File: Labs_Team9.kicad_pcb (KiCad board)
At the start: 2 copper layers, 101.7 x 39.2 mm, 51 parts, among them J1 Conn_02x04_Counter_Clockwise, J2 Conn_01x03_Pin, J3 Conn_01x04_Pin, J4 Conn_01x04_Pin, J5 USB_C_Receptacle_PowerOnly_6P, SW1 SW_Push, SW2 SW_Push, SW3 SW_Push, SW4 SW_Push, SW5 SW_Push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

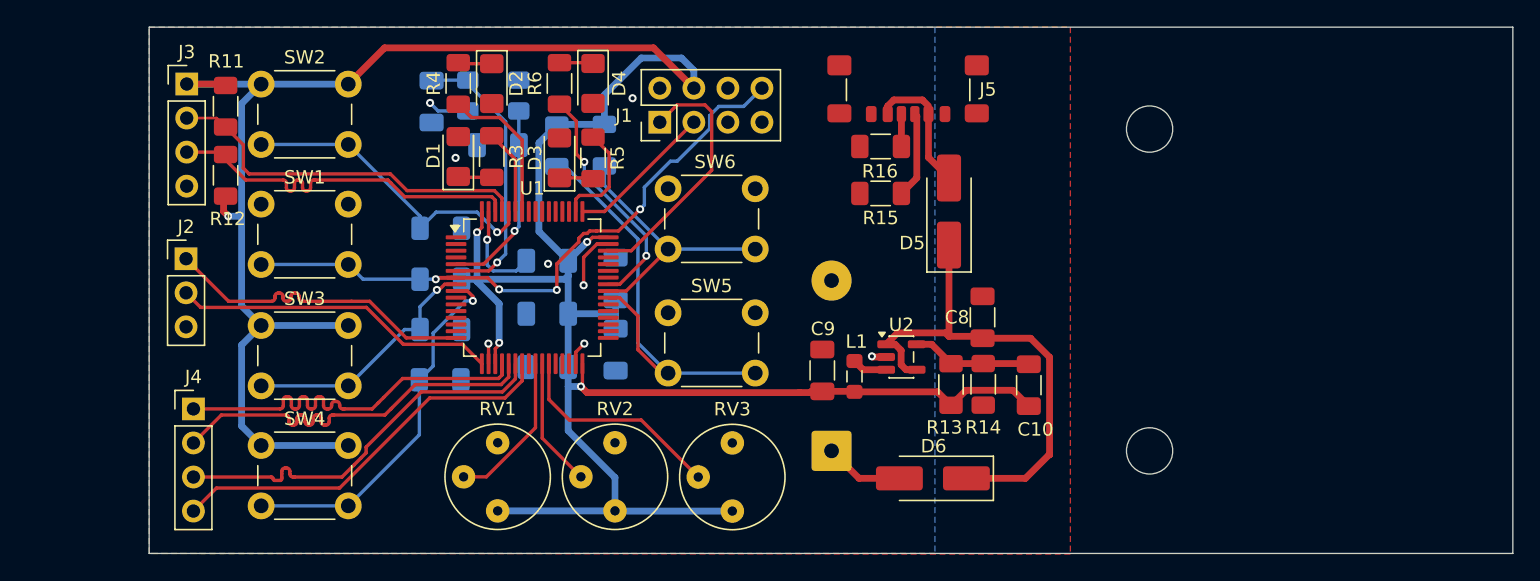
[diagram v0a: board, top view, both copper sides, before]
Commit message: lab5: add full tracing
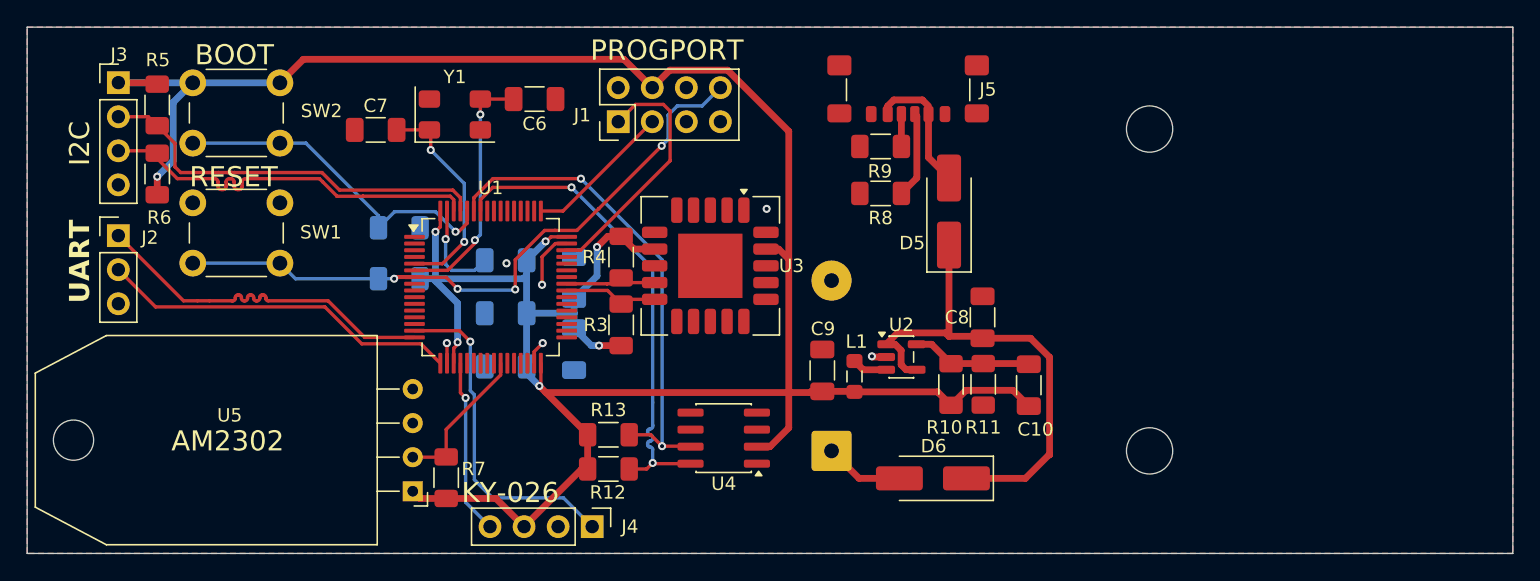
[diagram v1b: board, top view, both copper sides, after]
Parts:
- removed D1, D2, D3, D4: LED, LED_SMD:LED_1206_3216Metric_Pad1.42x1.75mm_HandSolder
- removed the R10 at (159.0, 90.2)
- removed the R5 at (158.2, 91.2)
- removed the R6 at (155.7, 85.7)
- removed the R8 at (146.8, 107.8)
- removed the R9 at (155.4, 90.3)
- removed RV1, RV2, RV3: R_Potentiometer, Potentiometer_THT:Potentiometer_Bourns_3339P_Vertical_HandSoldering
- removed SW3, SW4, SW5, SW6: SW_Push, Buttons_Switches_THT:SW_PUSH_6mm
- added R12: 2.2 kOhm, Resistor_SMD:R_1206_3216Metric_Pad1.30x1.75mm_HandSolder, F.Cu at (159.3, 114.4)
- added R13: 2.2 kOhm, Resistor_SMD:R_1206_3216Metric_Pad1.30x1.75mm_HandSolder, F.Cu at (159.3, 111.8)
- added U3: SCD40-D-R2, Sensor:Sensirion_SCD4x-1EP_10.1x10.1mm_P1.25mm_EP4.8x4.8mm, F.Cu at (166.9, 99.2)
- added U4: DS3231MZ, Package_SO:SOIC-8_3.9x4.9mm_P1.27mm, F.Cu at (167.9, 112.1)
- added U5: AM2302, Sensor:ASAIR_AM2302_P2.54mm_Lead2.75mm_TabDown, F.Cu at (144.7, 116.1)
- C6, C7, Y1: moved to F.Cu
- R3: value 510 Ohm -> 10 kOhm
- R4: value 680 Ohm -> 10 kOhm
- R7: value 10 kOhm -> 5.1 kOhm; moved to F.Cu
- moved J4 31.0 mm to (158.1, 118.7), turned to -90 degrees
- moved R4 17.8 mm to (160.2, 98.6), turned to -90 degrees
- moved R3 15.8 mm to (160.2, 103.7), turned to 90 degrees
- moved R7 11.1 mm to (147.2, 115.0), turned to 90 degrees
- moved C7 9.19 mm to (141.9, 89.1)
- moved C6 7.68 mm to (153.8, 86.8), turned to 180 degrees
- moved J2 5.34 mm to (122.8, 97.0)
- moved J3 5.10 mm to (122.8, 85.6)
- moved R5 5.10 mm to (125.7, 87.2)
- moved R6 5.10 mm to (125.7, 92.4)
- moved SW1 5.10 mm to (128.3, 94.5)
- moved SW2 5.10 mm to (134.8, 90.1)
- moved Y1 3.19 mm to (147.8, 88.0), turned to 0 degrees
- moved C2 3.10 mm to (151.6, 102.8)
- moved R2 3.10 mm to (143.7, 96.4)
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- renumbered R13 to R10, R14 to R11, R11 to R5, R12 to R6, R15 to R8, R16 to R9
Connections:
- J4 pad 1: SPI_NSS -> FLAME_ADC
- J4 pad 2: SPI_SCK -> GND
- J4 pad 3: SPI_MISO -> +3.3V
- J4 pad 4: SPI_MOSI -> FLAME_DATA
- R3 pad 1: Led_Green -> +3.3V
- R3 pad 2: Net-(D1-K) -> I2C2_SDA
- R4 pad 1: Led_Orange -> +3.3V
- R4 pad 2: Net-(D2-K) -> I2C2_SCL
- R7 pad 1: USERB1 -> +3.3V
- R7 pad 2: GND -> DATA_AM2302
- U1 pad 15: unconnected-(U1-PA1-Pad15) -> FLAME_ADC
- U1 pad 20: SPI_NSS -> FLAME_DATA
- U1 pad 21: SPI_SCK -> unconnected-(U1-PA5-Pad21)
- U1 pad 22: SPI_MISO -> unconnected-(U1-PA6-Pad22)
- U1 pad 23: SPI_MOSI -> unconnected-(U1-PA7-Pad23)
- U1 pad 25: ADC_MCU_1 -> unconnected-(U1-PC5-Pad25)
- U1 pad 26: ADC_MCU_2 -> DATA_AM2302
- U1 pad 27: ADC_MCU_3 -> unconnected-(U1-PB1-Pad27)
- U1 pad 39: USERB3 -> unconnected-(U1-PC8-Pad39)
- U1 pad 40: USERB4 -> I2C2_SDA
- U1 pad 41: Led_Blue -> I2C2_SCL
- U1 pad 50: Led_Red -> unconnected-(U1-PA15-Pad50)
- U1 pad 58: Led_Orange -> I2C3_SCL
- U1 pad 59: Led_Green -> I2C3_SDA
- U1 pad 8: USERB1 -> unconnected-(U1-PC0-Pad8)
- U1 pad 9: USERB2 -> unconnected-(U1-PC1-Pad9)
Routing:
- net I2C3_SDA: track 0.00 -> 37.0 mm, vias 0 -> 2
- net I2C3_SCL: track 0.00 -> 36.7 mm, vias 0 -> 2
- net USERB3: track 34.0 -> 0.00 mm
- net SPI_MOSI: track 29.8 -> 0.00 mm
- net SPI_MISO: track 29.8 -> 0.00 mm
- net SPI_SCK: track 29.7 -> 0.00 mm
- net SPI_NSS: track 29.6 -> 0.00 mm
- net USERB2: track 27.7 -> 0.00 mm, vias 1 -> 0
- net FLAME_ADC: track 0.00 -> 25.2 mm, vias 0 -> 1
- net USERB4: track 20.4 -> 0.00 mm
- net USERB1: track 18.7 -> 0.00 mm, vias 1 -> 0
- net Led_Blue: track 17.8 -> 0.00 mm, vias 2 -> 0
- net ADC_MCU_3: track 17.0 -> 0.00 mm
- net FLAME_DATA: track 0.00 -> 13.1 mm, vias 0 -> 1
- net ADC_MCU_1: track 11.7 -> 0.00 mm
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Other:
- board size 101.7 x 39.2 mm -> 110.8 x 39.2 mm
- board text added: "AM2302"
- board text added: "BOOT"
- board text added: "I2C"
- board text added: "KY-026"
- board text added: "PROGPORT"
- board text added: "RESET"
- board text added: "UART"
